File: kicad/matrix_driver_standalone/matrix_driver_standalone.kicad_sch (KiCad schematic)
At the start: 17 parts, among them J1 Conn_01x04, J2 Conn_01x04, U1 IS31FL3743A

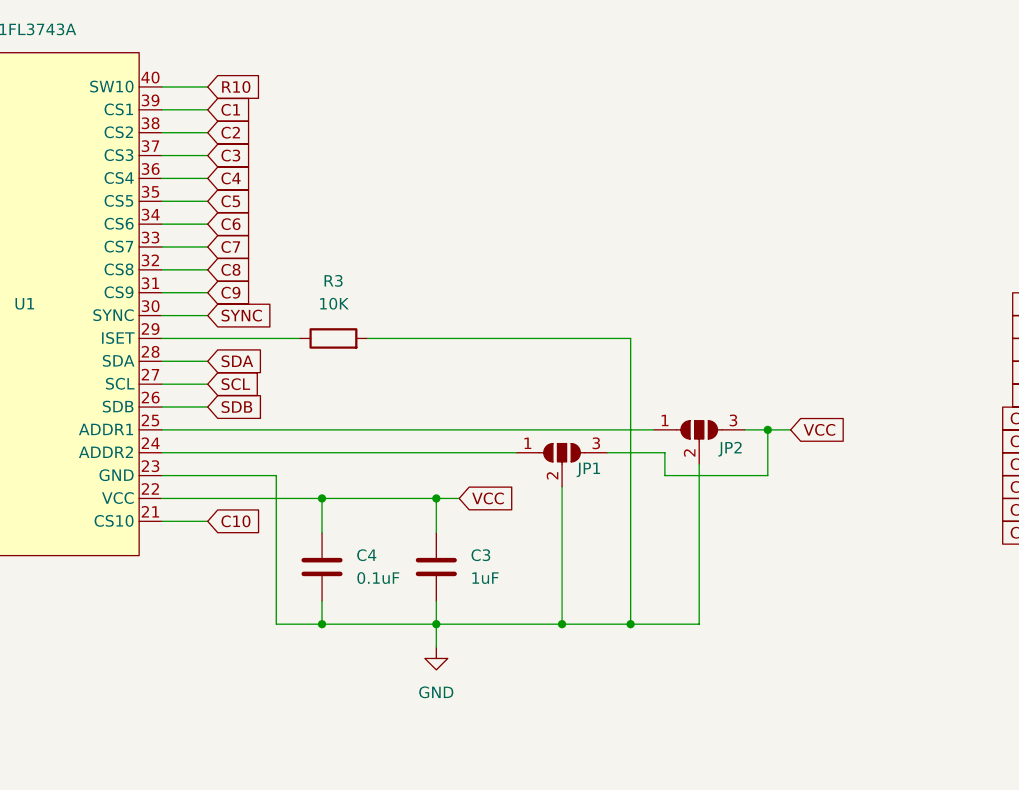
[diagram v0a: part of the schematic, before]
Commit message: play bad apple; fix an oopsie in the driver schematics/pcb
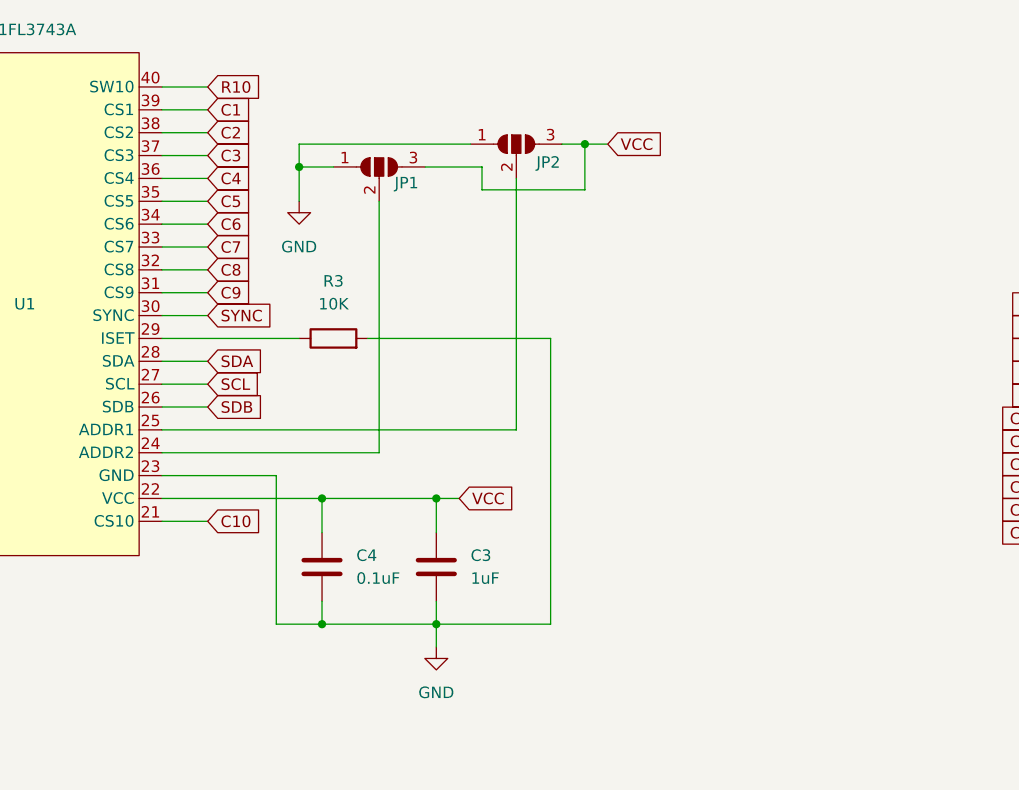
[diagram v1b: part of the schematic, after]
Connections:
- net GND: now also JP1.1 (A), JP2.1 (A); no longer JP1.2 (C), JP2.2 (C)
- net at U1.25 (ADDR1): now also JP2.2 (C); no longer JP2.1 (A)
- net at U1.24 (ADDR2): now also JP1.2 (C); no longer JP1.1 (A)
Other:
- moved on the sheet: JP1, JP2
